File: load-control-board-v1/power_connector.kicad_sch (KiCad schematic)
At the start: 2 parts, among them U4 TT56145145-1520, U9 TT56145145-1520

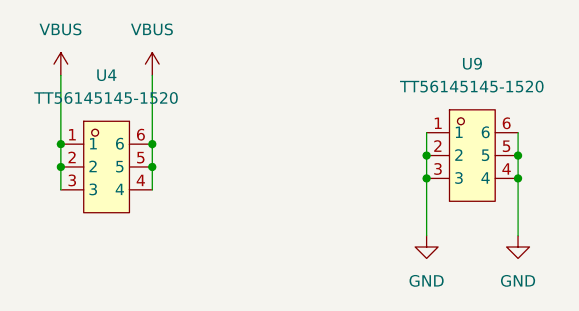
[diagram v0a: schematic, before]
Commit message: Add filled zone for mosfet, change terminal to from THO to SMT
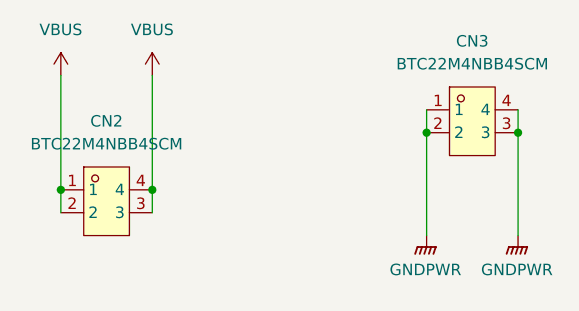
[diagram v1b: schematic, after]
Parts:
- removed U4, U9: TT56145145-1520, programmable-load-library:TH_6P-TT56145145-1500, symbol programmable-load-library:TT56145145-1520
- added CN2, CN3: BTC22M4NBB4SCM, programmable-load-library:CONN-SMD_L10.8-W10.0-LS17.4, symbol programmable-load-library:BTC22M4NBB4SCM
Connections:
- net VBUS: now also CN2.1, CN2.2, CN2.3, CN2.4
- new net GNDPWR: CN3.1, CN3.2, CN3.3, CN3.4
